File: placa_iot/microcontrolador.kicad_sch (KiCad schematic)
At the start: 0 parts

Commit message: Microcontrolador en proceso
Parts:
- added C10, C6: 1 uF, Capacitor_SMD:C_0402_1005Metric, symbol Device:C
- added C11, C12, C13, C8: 100 nF, Capacitor_SMD:C_0402_1005Metric, symbol Device:C
- added C14, C15: 12 pF, Capacitor_SMD:C_0402_1005Metric, symbol Device:C
- added C16, C17, C18, C19, C20, C21: NC, Capacitor_SMD:C_0402_1005Metric, symbol Device:C
- added C7: 10 nF, Capacitor_SMD:C_0402_1005Metric, symbol Device:C
- added C9: 10 uF, Capacitor_SMD:C_0402_1005Metric, symbol Device:C
- added L1: 2nH, Inductor_SMD:L_0402_1005Metric, symbol Device:L
- added L2: 22 nH, Inductor_SMD:L_0402_1005Metric, symbol Device:L
- added R4: NC, Resistor_SMD:R_0402_1005Metric, symbol Device:R
- added R5: 499, Resistor_SMD:R_0402_1005Metric, symbol Device:R
- added U3: ESP32-S3, ic_control:QFN-56-1EP_7x7mm_P0.4mm_EP4x4mm, symbol ic_control:ESP32-S3
- added U4: PRO-OB-536, antennas:ANTENNA_PIFA_3D_2.4GHZ, symbol Antenas:ANTENNA_PIFA_3D_2.4GHZ
- added Y1: 40 MHz, Crystal:Crystal_SMD_3225-4Pin_3.2x2.5mm, symbol Device:Crystal_GND24
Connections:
- new net: C20.2, C21.1, U4.2 (FEED)
- new net: C14.1, L2.1, Y1.1
- new net: C15.1, U3.53 (XTAL_N), Y1.3
- new net: R5.2, U3.49 (U0TXD)
- new net: C12.1, L1.2, U3.2 (VDD3P3), U3.3 (VDD3P3)
- new net: C16.1, C17.1, C18.1, C18.2, C19.1, C20.1, U3.1 (LNA_IN)
- new net: L2.2, U3.54 (XTAL_P)
- new net +3.3V: C10.1, C11.1, C13.1, C6.1, C7.1, C8.1, C9.1, L1.1, R4.2, U3.20 (VDD3P3_RTC), U3.46 (VDD3P3_CPU), U3.55 (VDDA), U3.56 (VDDA)
- new net CMD-M0S1-IO11: U3.16 (GPIO11)
- new net GND: C10.2, C11.2, C12.2, C13.2, C14.2, C15.2, C16.2, C17.2, C19.2, C21.2, C6.2, C7.2, C8.2, C9.2, U3.57 (GND), U4.1 (GND), Y1.2 (G), Y1.4 (G)
- new net IO0: U3.5 (GPIO0)
- new net IO1: U3.6 (GPIO1)
- new net IO15: U3.21 (XTAL_32K_P)
- new net IO16: U3.22 (XTAL_32K_N)
- new net IO3: U3.8 (GPIO3)
- new net IO38: U3.43 (GPIO38)
- new net IO39/MTC: U3.44 (MTCK)
- new net IO4: U3.9 (GPIO4)
- new net IO40/MTDO: U3.45 (MTDO)
- new net IO41/MTDI: U3.47 (MTDI)
- new net IO42/MTMS: U3.48 (MTMS)
- new net IO45: R4.1, U3.51 (GPIO45)
- new net IO46: U3.52 (GPIO46)
- new net IO5: U3.10 (GPIO5)
- new net IO6: U3.11 (GPIO6)
- new net IO7: U3.12 (GPIO7)
- new net IO8: U3.13 (GPIO8)
- new net IO9: U3.14 (GPIO9)
- new net LORA_TX: U3.15 (GPIO10)
- new net RST/EN: U3.4 (CHIP_PU)
- new net SD0-MISO-IO2: U3.7 (GPIO2)
- new net U0RXD: U3.50 (U0RXD)
- new net U0TXD: R5.1
- no-connect marks 0 -> 11

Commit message: Bloque microcontrolador terminado
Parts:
- added C22: 1 uF, Capacitor_SMD:C_0402_1005Metric, symbol Device:C
- added J1, J2: 22-28-4144, connectors:CONN_THT_MV_PH_P2.54MM_P14, symbol connectors:CONN_THT_MV_PH_P2.54MM_P14
- added R6, R8: 10 k, Resistor_SMD:R_0402_1005Metric, symbol Device:R
- added R7: 0R, Resistor_SMD:R_0402_1005Metric, symbol Device:R
- added SW1: RST/EN, Button_Switch_SMD:SW_Push_SPST_NO_Alps_SKRK, symbol Switch:SW_Push
- added SW2: BOOT, Button_Switch_SMD:SW_Push_SPST_NO_Alps_SKRK, symbol Switch:SW_Push
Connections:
- net +3.3V: now also R6.2, R8.2
- net GND: now also C22.2, J1.2 (Pin_2), J1.4 (Pin_4), J2.14 (Pin_14), SW1.1, SW2.1
- net IO0: now also J2.3 (Pin_3), R8.1, SW2.2
- net IO15: now also J2.12 (Pin_12)
- net IO16: now also J2.13 (Pin_13)
- net IO38: now also J1.13 (Pin_13)
- net IO40/MTDO: now also J1.9 (Pin_9)
- net IO41/MTDI: now also J1.8 (Pin_8)
- net IO42/MTMS: now also J1.5 (Pin_5)
- net IO45: now also J1.7 (Pin_7)
- net IO46: now also J1.6 (Pin_6)
- net IO8: now also J2.9 (Pin_9)
- net RST/EN: now also C22.1, J2.11 (Pin_11), R6.1, R7.1
- net U0RXD: now also J1.11 (Pin_11)
- net U0TXD: now also J1.12 (Pin_12)
- net IO12: now reaches U3.17 (GPIO12)
- net IO12: now also J2.10 (Pin_10)
- net SD3-CS-IO13: now reaches U3.18 (GPIO13)
- net CLK-SCK-IO14: now reaches U3.19 (GPIO14)
- net IO17: now reaches U3.23 (GPIO17)
- net IO18: now reaches U3.24 (GPIO18)
- net DM: now reaches U3.25 (GPIO19/USB_D-)
- net DP: now reaches U3.26 (GPIO20/USB_D+)
- net LORA_RX: now reaches U3.27 (GPIO21)
- net IO48: now reaches U3.36 (SPICLK_N)
- net IO48: now also J2.8 (Pin_8)
- net IO47: now reaches U3.37 (SPICLK_P)
- net IO47: now also J2.7 (Pin_7)
- net IO33: now reaches U3.38 (GPIO33)
- net IO33: now also J2.6 (Pin_6)
- net IO34: now reaches U3.39 (GPIO34)
- net IO34: now also J2.5 (Pin_5)
- net IO35: now reaches U3.40 (GPIO35)
- net IO35: now also J2.4 (Pin_4)
- net IO36: now reaches U3.41 (GPIO36)
- net IO36: now also J2.2 (Pin_2)
- net IO37: now reaches U3.42 (GPIO37)
- net IO37: now also J2.1 (Pin_1)
- net IO39/MTC renamed IO39/MTCK
- net IO39/MTCK: now also J1.10 (Pin_10)
- new net: R7.2, SW1.2
- new net VBAT: J1.14 (Pin_14)
- new net VBUS: J1.1 (Pin_1)
- new net Vcc+3.3: J1.3 (Pin_3)
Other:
- moved on the sheet: C10, C11, C12, C13, C14, C15, C16, C17, C18, C19, C20, C21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

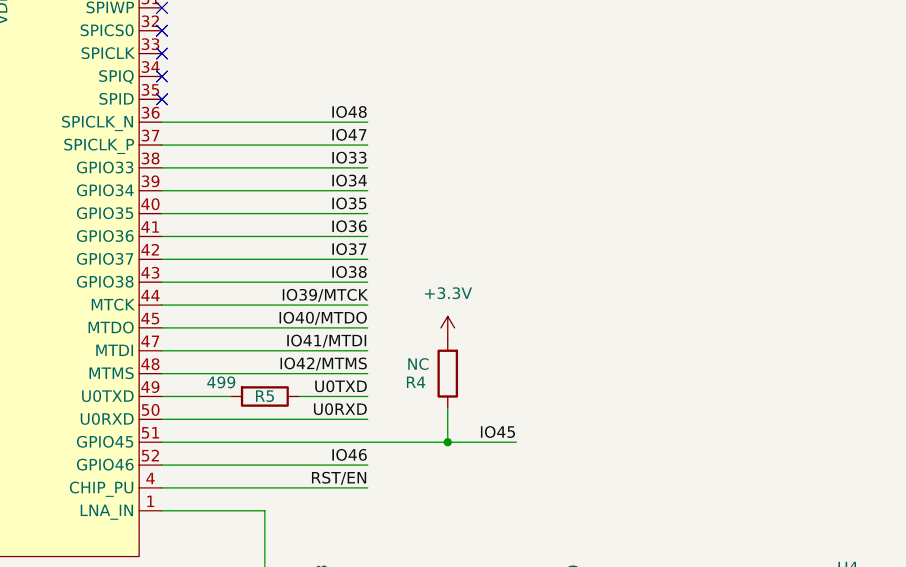
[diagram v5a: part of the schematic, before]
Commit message: Esquemático USB completado
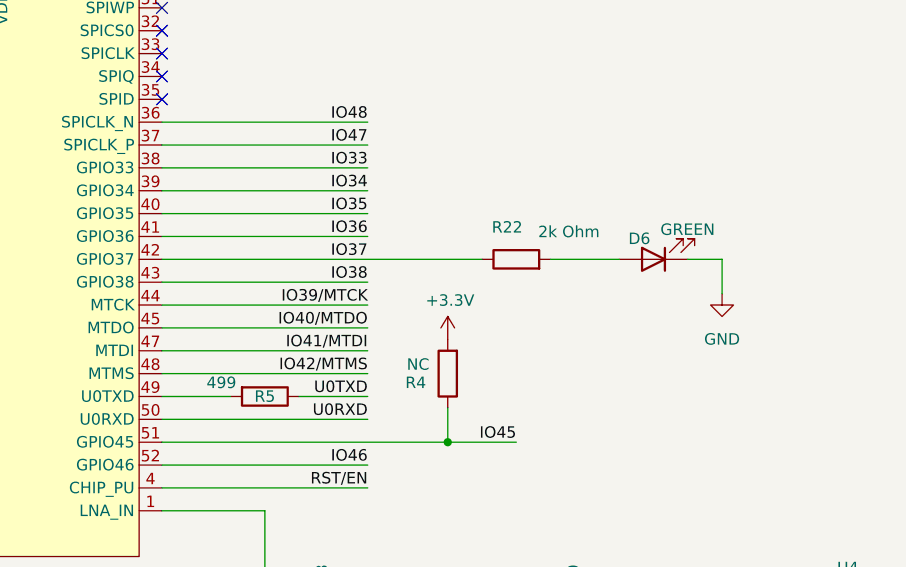
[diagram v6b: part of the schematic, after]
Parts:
- added D6: GREEN, LED_SMD:LED_0402_1005Metric, symbol Device:LED
- added R22: 2k Ohm, Resistor_SMD:R_0402_1005Metric, symbol Device:R
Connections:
- net GND: now also D6.1 (K)
- net IO37: now also R22.1
- new net: D6.2 (A), R22.2

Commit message: Esquemático acabado
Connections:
- net DM renamed D+
- net DP renamed D-

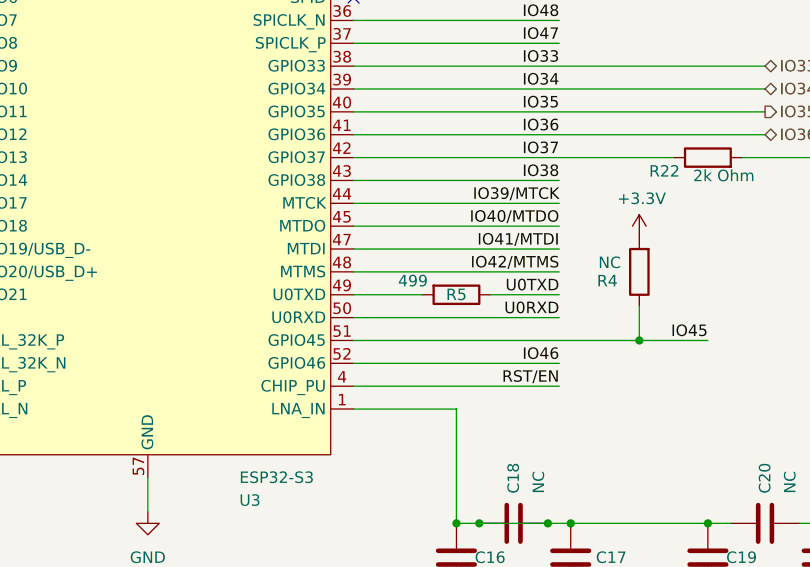
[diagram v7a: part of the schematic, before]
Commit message: Layout iniciado y resolución de errores de huellas
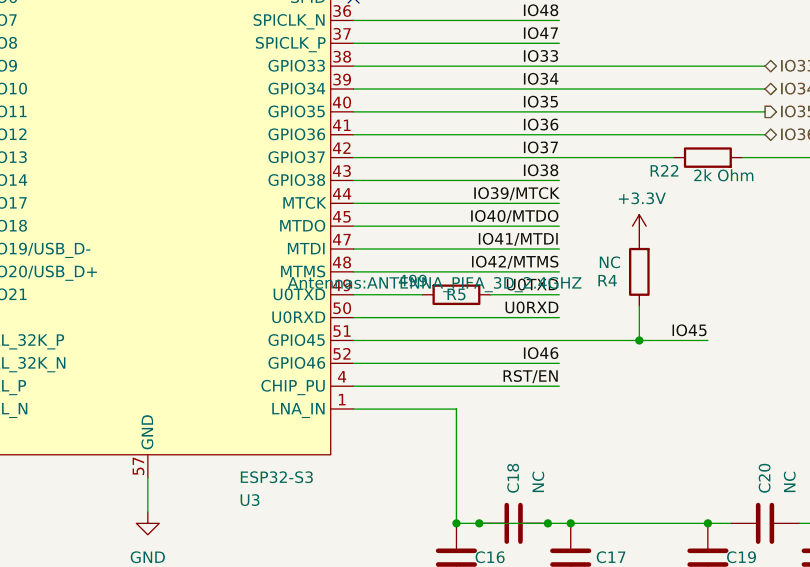
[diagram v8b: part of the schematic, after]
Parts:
- J1, J2: footprint connectors:CONN_THT_MV_PH_P2.54MM_P14 -> Connectors:CONN_THT_MV_PH_P2.54MM_P14
- U4: footprint antennas:ANTENNA_PIFA_3D_2.4GHZ -> Antennas:ANTENNA_PIFA_3D_2.4GHZ
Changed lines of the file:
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@@
 			)
 		)
-		(property "Footprint" "antennas:ANTENNA_PIFA_3D_2.4GHZ"
+		(property "Footprint" "Antennas:ANTENNA_PIFA_3D_2.4GHZ"
 			(at 257.81 162.56 0)
-			(hide yes)
 			(show_name no)
 			(do_not_autoplace yes)
@@
 			)
 		)
-		(property "Footprint" "connectors:CONN_THT_MV_PH_P2.54MM_P14"
+		(property "Footprint" "Connectors:CONN_THT_MV_PH_P2.54MM_P14"
 			(at 138.43 97.79 0)
 			(hide yes)
@@
 			)
 		)
-		(property "Footprint" "connectors:CONN_THT_MV_PH_P2.54MM_P14"
+		(property "Footprint" "Connectors:CONN_THT_MV_PH_P2.54MM_P14"
 			(at 138.43 144.78 0)
 			(hide yes)
